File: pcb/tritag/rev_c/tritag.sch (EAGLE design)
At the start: 135 parts, among them J1 TC2030-JLINK-NL, J2 TC2030-JLINK-NL, J3 MICRO_USB_B_HIROSE_ZX62-B-5PA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, J5 BAT_HOLE, J7 CON_MICRO_SDDM3AT-SF-PEJM5, T1 HHM1595A1, U1 NRF52840, U12 SIP32510, U2 MCP73831, U3 FT232RQ, U4 MAX8887EZK33+T, U5 STM32F091CC, U6 SKY13317, U7 LXDC2HN18A, U8 DW1000, U9 LIS2DW12, X1 32MHz, X2 38.4M, X3 16M, X4 32.768kHz

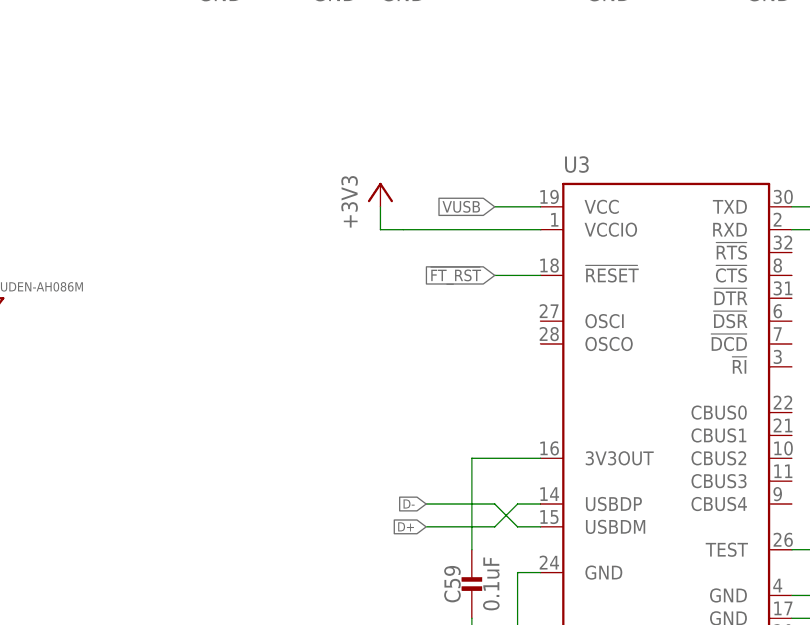
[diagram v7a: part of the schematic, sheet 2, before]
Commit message: moved BLE antenna and accelerometer and cleaned up nRF connections
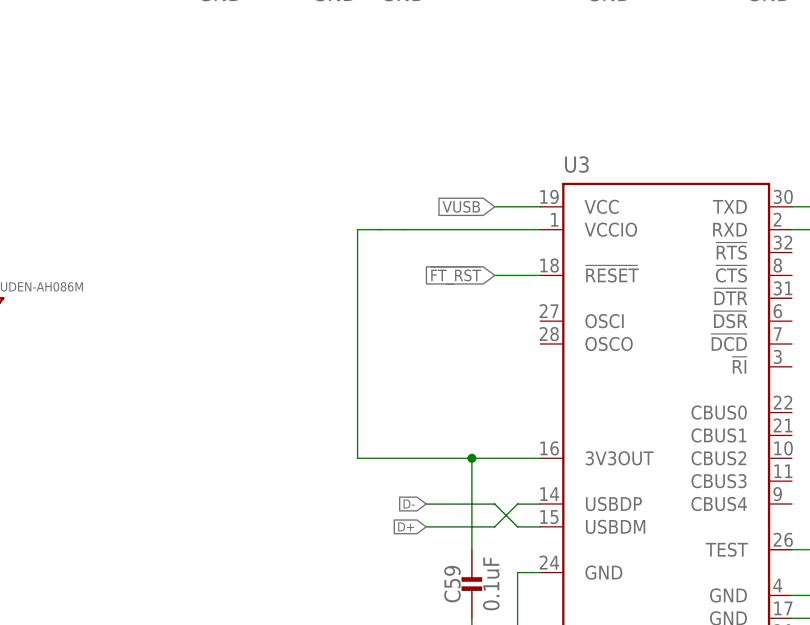
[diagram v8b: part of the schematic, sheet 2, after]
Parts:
- GPIO0, GPIO1: value TEST_POINT_0.040IN -> TEST-POINT; device headers:TEST_POINT_0.040IN -> headers:TEST-POINT
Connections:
- net +3V3: no longer U3.VCCIO
- net N$1: now also U3.VCCIO
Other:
- note removed: "PC Test Points"
- note removed: "Pad Test Points"
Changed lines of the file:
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@@
 <attribute name="MPN" value="GRM155R71C104KA88J "/>
 </part>
-<part name="P+21" library="regulators" deviceset="+3V3" device=""/>
 <part name="U9" library="chips" deviceset="LIS2DW12" device=""/>
 <part name="C75" library="passives" deviceset="CAPACITOR" device="0402_CAP" value="0.1uF">
@@
 <part name="D2" library="leds" deviceset="SML-LX0404SIUPGUSB" device=""/>
 <part name="R13" library="passives" deviceset="RESISTOR" device="0402_RES" value="1k"/>
-<part name="GPIO0" library="headers" deviceset="TEST_POINT_0.040IN" device=""/>
-<part name="GPIO1" library="headers" deviceset="TEST_POINT_0.040IN" device=""/>
+<part name="GPIO0" library="headers" deviceset="TEST-POINT" device=""/>
+<part name="GPIO1" library="headers" deviceset="TEST-POINT" device=""/>
 <part name="TP5" library="headers" deviceset="TEST-POINT" device=""/>
 <part name="TP6" library="headers" deviceset="TEST-POINT" device=""/>
@@
 <attribute name="MPN" x="185.42" y="60.96" size="1.778" layer="96" display="off"/>
 </instance>
-<instance part="P+21" gate="P1" x="175.26" y="104.14"/>
 <instance part="U9" gate="G$1" x="30.48" y="66.04"/>
 <instance part="C75" gate="G$1" x="40.64" y="104.14">
@@
 <junction x="243.84" y="160.02"/>
 <pinref part="U4" gate="G$1" pin="OUT"/>
-</segment>
-<segment>
-<pinref part="P+21" gate="P1" pin="+3V3"/>
-<wire x1="175.26" y1="99.06" x2="175.26" y2="101.6" width="0.1524" layer="91"/>
-<pinref part="U3" gate="1" pin="VCCIO"/>
-<wire x1="193.04" y1="99.06" x2="177.8" y2="99.06" width="0.1524" layer="91"/>
-<wire x1="177.8" y1="99.06" x2="175.26" y2="99.06" width="0.1524" layer="91"/>
 </segment>
 <segment>
@@
 <wire x1="231.14" y1="154.94" x2="233.68" y2="154.94" width="0.1524" layer="91"/>
 <wire x1="233.68" y1="154.94" x2="233.68" y2="152.4" width="0.1524" layer="91"/>
-</segment>
-</net>
-<net name="N$1" class="0">
-<segment>
-<pinref part="U3" gate="1" pin="3V3OUT"/>
-<wire x1="193.04" y1="73.66" x2="185.42" y2="73.66" width="0.1524" layer="91"/>
-<pinref part="C59" gate="G$1" pin="1"/>
-<wire x1="185.42" y1="73.66" x2="185.42" y2="63.5" width="0.1524" layer="91"/>
 </segment>
 </net>
@@
 </segment>
 </net>
+<net name="N$1" class="0">
+<segment>
+<pinref part="U3" gate="1" pin="VCCIO"/>
+<wire x1="193.04" y1="99.06" x2="177.8" y2="99.06" width="0.1524" layer="91"/>
+<wire x1="177.8" y1="99.06" x2="175.26" y2="99.06" width="0.1524" layer="91"/>
+<wire x1="175.26" y1="99.06" x2="172.72" y2="99.06" width="0.1524" layer="91"/>
+<wire x1="172.72" y1="99.06" x2="172.72" y2="73.66" width="0.1524" layer="91"/>
+<pinref part="U3" gate="1" pin="3V3OUT"/>
+<wire x1="193.04" y1="73.66" x2="185.42" y2="73.66" width="0.1524" layer="91"/>
+<pinref part="C59" gate="G$1" pin="1"/>
+<wire x1="185.42" y1="73.66" x2="185.42" y2="63.5" width="0.1524" layer="91"/>
+<wire x1="172.72" y1="73.66" x2="185.42" y2="73.66" width="0.1524" layer="91"/>
+<junction x="185.42" y="73.66"/>
+</segment>
+</net>
 </nets>
 </sheet>
@@
 <text x="7.62" y="121.92" size="3.81" layer="98">STM32F091CC</text>
 <text x="228.6" y="180.34" size="3.81" layer="98">DW1000</text>
-<text x="114.3" y="142.24" size="3.81" layer="98">RF + DCDC</text>
+<text x="111.76" y="142.24" size="3.81" layer="98">RF + DCDC</text>
 <wire x1="144.78" y1="134.62" x2="144.78" y2="190.5" width="0.1524" layer="98" style="longdash"/>
-<text x="112.776" y="116.586" size="1.27" layer="98">I2C: Pull-up
+<text x="115.316" y="116.586" size="1.27" layer="98">I2C: Pull-up
 resistor required</text>
-<text x="114.3" y="73.66" size="0.762" layer="98">PC
-Test Points</text>
-<text x="101.6" y="47.498" size="0.762" layer="98">Pad
-Test Points</text>
 <text x="129.54" y="30.48" size="2.032" layer="98">LED</text>
 <text x="57.15" y="110.236" size="0.762" layer="98" rot="R90">INTERRUPT: used both for waking up
 from STOP (USART2_TX)
 and STANDBY (WKUP4)</text>
-<text x="241.3" y="159.258" size="1.016" layer="98" rot="R90">Pull-down
+<text x="241.3" y="157.988" size="1.016" layer="98" rot="R90">Pull-down
 for (DEEP)SLEEP</text>
 <text x="66.04" y="25.4" size="2.032" layer="98" rot="R90">VDD/48</text>
